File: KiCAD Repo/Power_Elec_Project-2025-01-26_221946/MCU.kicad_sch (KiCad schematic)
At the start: 0 parts

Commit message: test
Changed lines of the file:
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@@
 	(hierarchical_label "VFILT"
 		(shape input)
-		(at 88.9 33.02 0)
+		(at 88.9 31.75 180)
 		(effects
 			(font
 				(size 1.27 1.27)
 			)
-			(justify left)
+			(justify right)
 		)
 	)

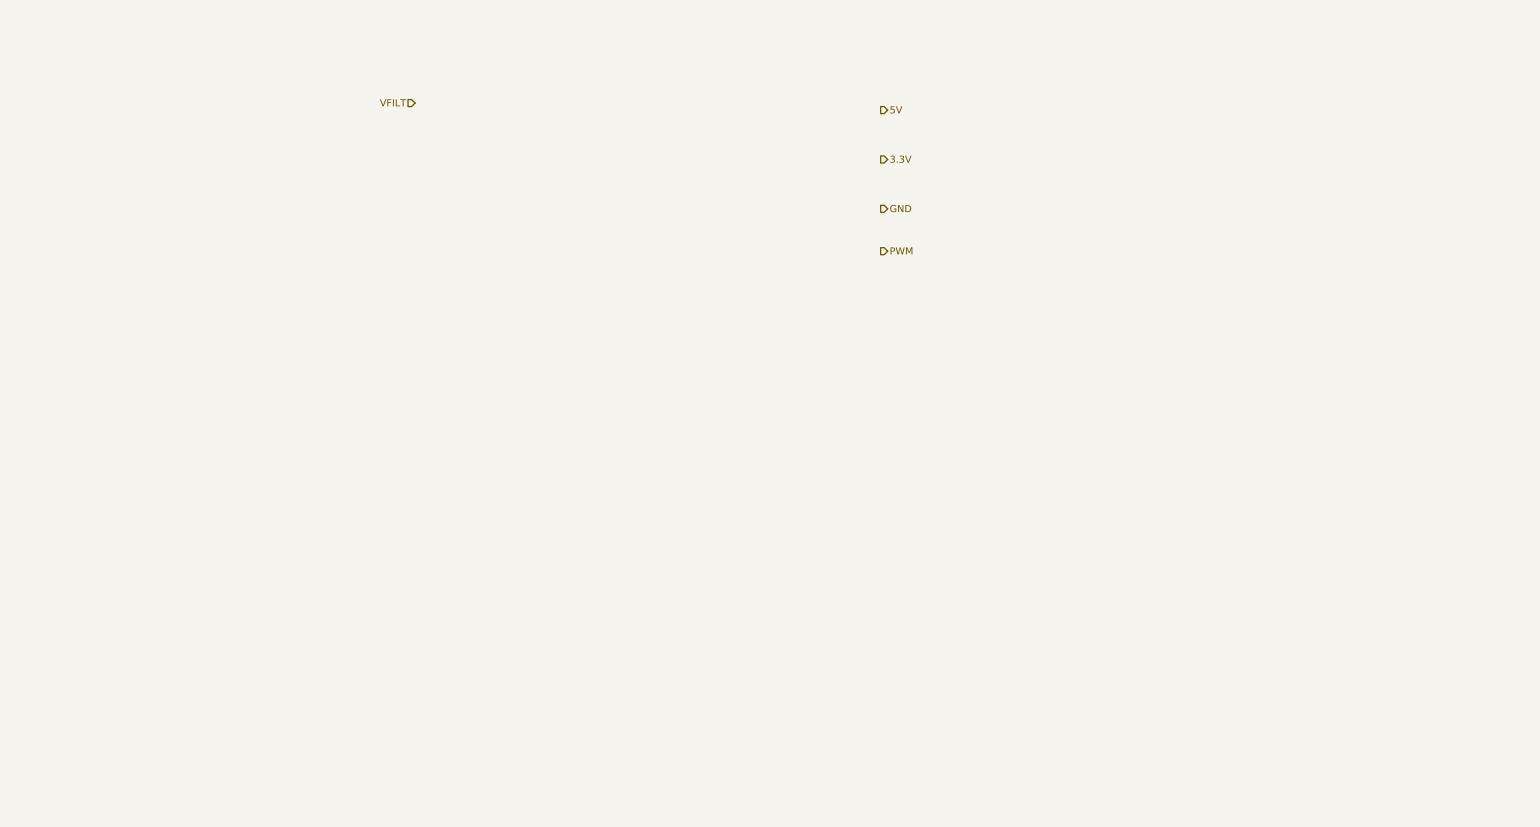
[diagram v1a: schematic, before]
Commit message: Added MCU footprint
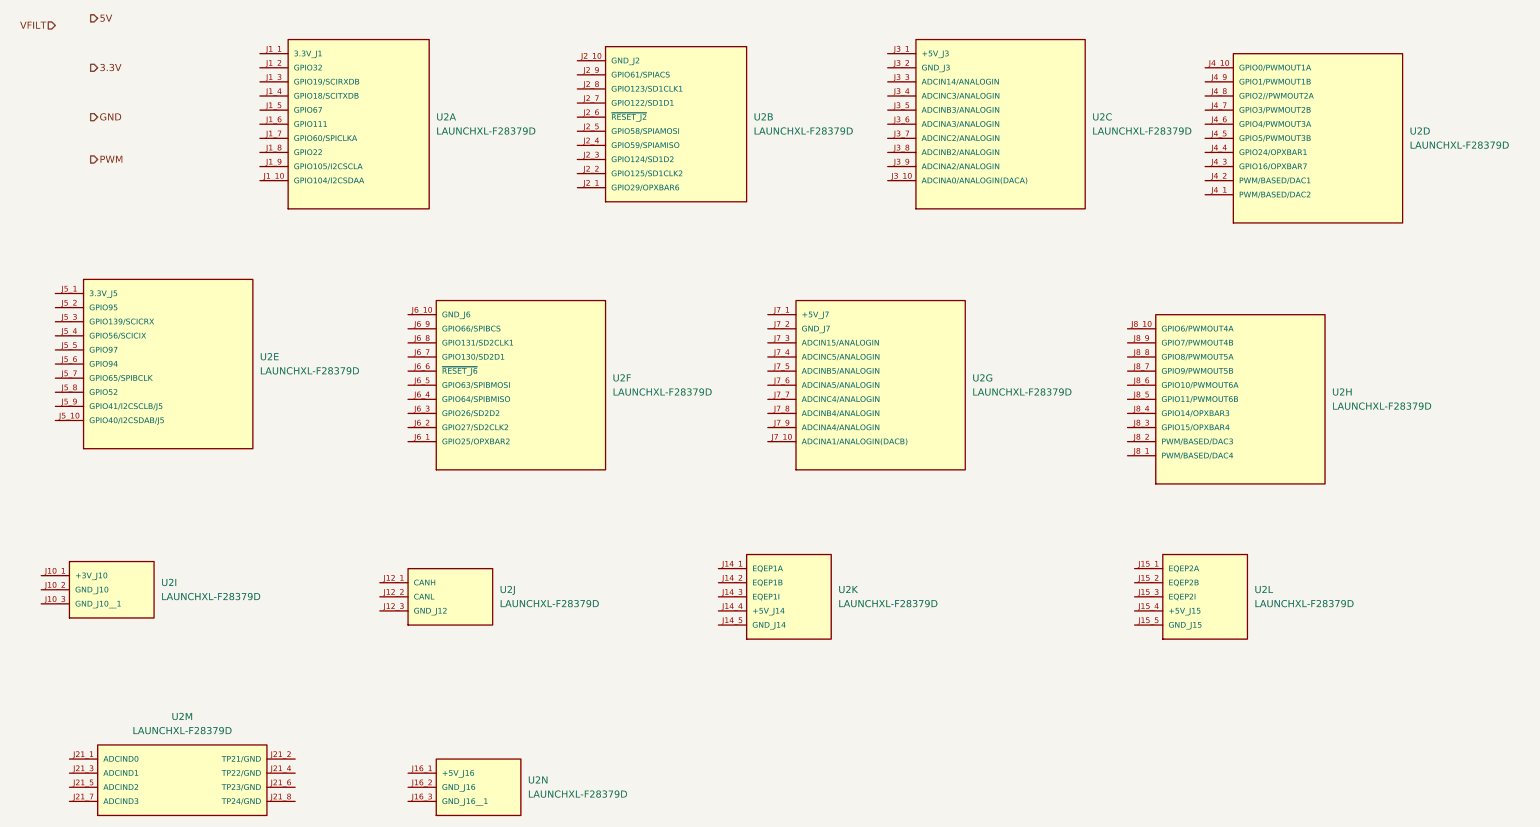
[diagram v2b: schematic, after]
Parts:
- added U2: LAUNCHXL-F28379D, F28379D:MOD_LAUNCHXL-F28379D, symbol LAUNCHXL-F28379D:LAUNCHXL-F28379D

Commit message: PLF and GD circuit
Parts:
- U2: Part Number (none) -> LAUNCHXL-F28379D
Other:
- company: (none) -> M.Nguyen B.Patel S.Dupuis
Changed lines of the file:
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@@
 	(generator_version "8.0")
 	(paper "A4")
+	(title_block
+		(date "2025-02-21")
+		(rev "1")
+		(company "M.Nguyen B.Patel S.Dupuis")
+	)
 	(hierarchical_label "3.3V"
 		(shape output)
@@
 			)
 		)
+		(property "Part Number" "LAUNCHXL-F28379D"
+			(at 34.29 116.84 0)
+			(effects
+				(font
+					(size 1.27 1.27)
+				)
+				(hide yes)
+			)
+		)
 		(pin "J4_6"
 		)
@@
 			)
 		)
+		(property "Part Number" "LAUNCHXL-F28379D"
+			(at 237.49 85.09 0)
+			(effects
+				(font
+					(size 1.27 1.27)
+				)
+				(hide yes)
+			)
+		)
 		(pin "J4_6"
 		)
@@
 			)
 		)
+		(property "Part Number" "LAUNCHXL-F28379D"
+			(at 156.21 120.65 0)
+			(effects
+				(font
+					(size 1.27 1.27)
+				)
+				(hide yes)
+			)
+		)
 		(pin "J4_6"
 		)
@@
 			)
 		)
+		(property "Part Number" "LAUNCHXL-F28379D"
+			(at 44.45 78.74 0)
+			(effects
+				(font
+					(size 1.27 1.27)
+				)
+				(hide yes)
+			)
+		)
 		(pin "J4_6"
 		)
@@
 			)
 		)
+		(property "Part Number" "LAUNCHXL-F28379D"
+			(at 231.14 120.65 0)
+			(effects
+				(font
+					(size 1.27 1.27)
+				)
+				(hide yes)
+			)
+		)
 		(pin "J4_6"
 		)
@@
 			)
 		)
+		(property "Part Number" "LAUNCHXL-F28379D"
+			(at 251.46 38.1 0)
+			(effects
+				(font
+					(size 1.27 1.27)
+				)
+				(hide yes)
+			)
+		)
 		(pin "J4_6"
 		)
@@
 			)
 		)
+		(property "Part Number" "LAUNCHXL-F28379D"
+			(at 78.74 35.56 0)
+			(effects
+				(font
+					(size 1.27 1.27)
+				)
+				(hide yes)
+			)
+		)
 		(pin "J4_6"
 		)
@@
 			)
 		)
+		(property "Part Number" "LAUNCHXL-F28379D"
+			(at 46.99 152.4 0)
+			(effects
+				(font
+					(size 1.27 1.27)
+				)
+				(hide yes)
+			)
+		)
 		(pin "J4_6"
 		)
@@
 			)
 		)
+		(property "Part Number" "LAUNCHXL-F28379D"
+			(at 95.25 120.65 0)
+			(effects
+				(font
+					(size 1.27 1.27)
+				)
+				(hide yes)
+			)
+		)
 		(pin "J4_6"
 		)
@@
 			)
 		)
+		(property "Part Number" "LAUNCHXL-F28379D"
+			(at 107.95 82.55 0)
+			(effects
+				(font
+					(size 1.27 1.27)
+				)
+				(hide yes)
+			)
+		)
 		(pin "J4_6"
 		)
@@
 			)
 		)
+		(property "Part Number" "LAUNCHXL-F28379D"
+			(at 135.89 36.83 0)
+			(effects
+				(font
+					(size 1.27 1.27)
+				)
+				(hide yes)
+			)
+		)
 		(pin "J4_6"
 		)
@@
 			)
 		)
+		(property "Part Number" "LAUNCHXL-F28379D"
+			(at 172.72 82.55 0)
+			(effects
+				(font
+					(size 1.27 1.27)
+				)
+				(hide yes)
+			)
+		)
 		(pin "J4_6"
 		)
@@
 			)
 		)
+		(property "Part Number" "LAUNCHXL-F28379D"
+			(at 194.31 35.56 0)
+			(effects
+				(font
+					(size 1.27 1.27)
+				)
+				(hide yes)
+			)
+		)
 		(pin "J4_6"
 		)
@@
 				(hide yes)
 			)
+		)
+		(property "Part Number" "LAUNCHXL-F28379D"
+			(at 100.33 154.94 0)
+			(effects
+				(font
+					(size 1.27 1.27)
+				)
+				(hide yes)
+			)

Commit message: PCB
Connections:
- net GND: now also U2.J10_2 (GND_J10), U2.J10_3 (GND_J10__1), U2.J12_3 (GND_J12), U2.J14_5 (GND_J14), U2.J15_5 (GND_J15), U2.J16_2 (GND_J16), U2.J16_3 (GND_J16__1), U2.J21_2 (TP21/GND), U2.J21_4 (TP22/GND), U2.J21_6 (TP23/GND), U2.J21_8 (TP24/GND), U2.J2_10 (GND_J2), U2.J3_2 (GND_J3), U2.J7_2 (GND_J7)
- net PWM: now also U2.J8_5 (GPIO11/PWMOUT6B)
- net VFILT: now also U2.J3_3 (ADCIN14/ANALOGIN)
- net +3.3V: now reaches U2.J1_1 (3.3V_J1)
- net +5V: now reaches U2.J7_1 (+5V_J7)
- no-connect marks 0 -> 89
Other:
- moved on the sheet: U2I, U2N

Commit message: PCB fix
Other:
- moved on the sheet: U2F, U2G, U2H
